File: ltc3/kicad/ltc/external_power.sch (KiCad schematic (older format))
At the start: 44 parts, among them M501 1A, M502 1A, M503 1A, M504 1A, P503 MicroFit header, P504 MicroFit connector, P505 MicroFit header, P506 MicroFit connector, P507 PowerPole, P508 PowerPole, P509 PowerPole, P510 PowerPole, P511 PowerPole, P512 PowerPole, P513 PowerPole, P514 PowerPole, Q501 PMV45EN, Q502 PMV45EN, Q503 PMV45EN, Q504 PMV45EN, SW501 MOMENTARY, SW502 MOMENTARY, SW503 MOMENTARY, SW504 MOMENTARY, U501 TLP3542, U502 TLP3542, U503 TLP3542, U504 TLP3542

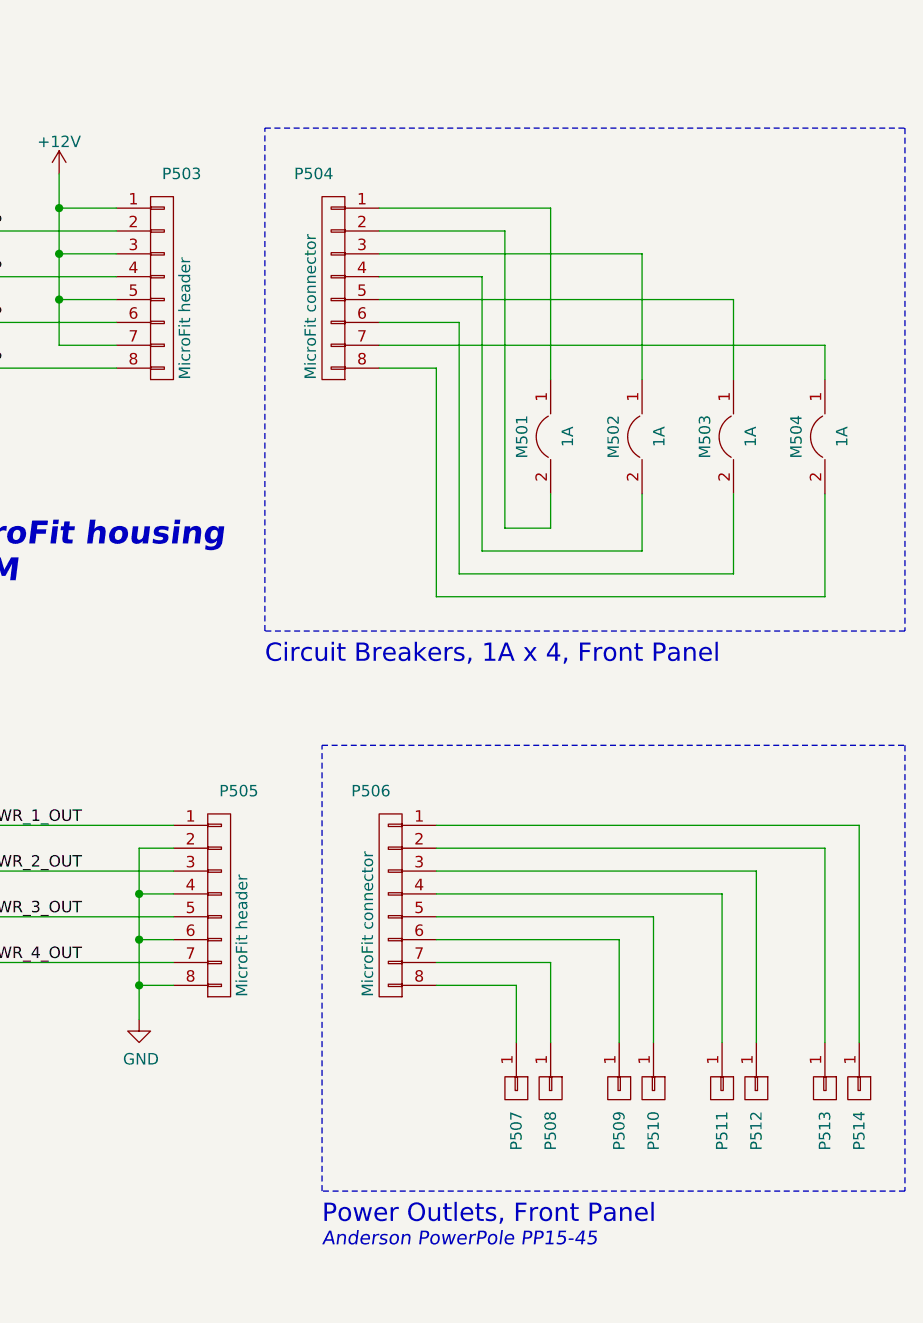
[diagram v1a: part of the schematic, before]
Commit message: LTC3: LTC BOM and PCB changes.
1. Added RJ45 connector outline to BeagleBone footprint.

2. Rotated BeagleBone footprint on PCB, so that the RJ45 connector
   is on a board edge.

3. Added a notch to the board for BeagleBone RJ45 jack clearance.

4. Updated PCB footprint annotations to align with changes made to the
   LTC schematic in the past few months.

5. Changed BAKERCON MOSFETs to be same part used to activate ignition
   relays.  (Fewer distinct components on the board.)
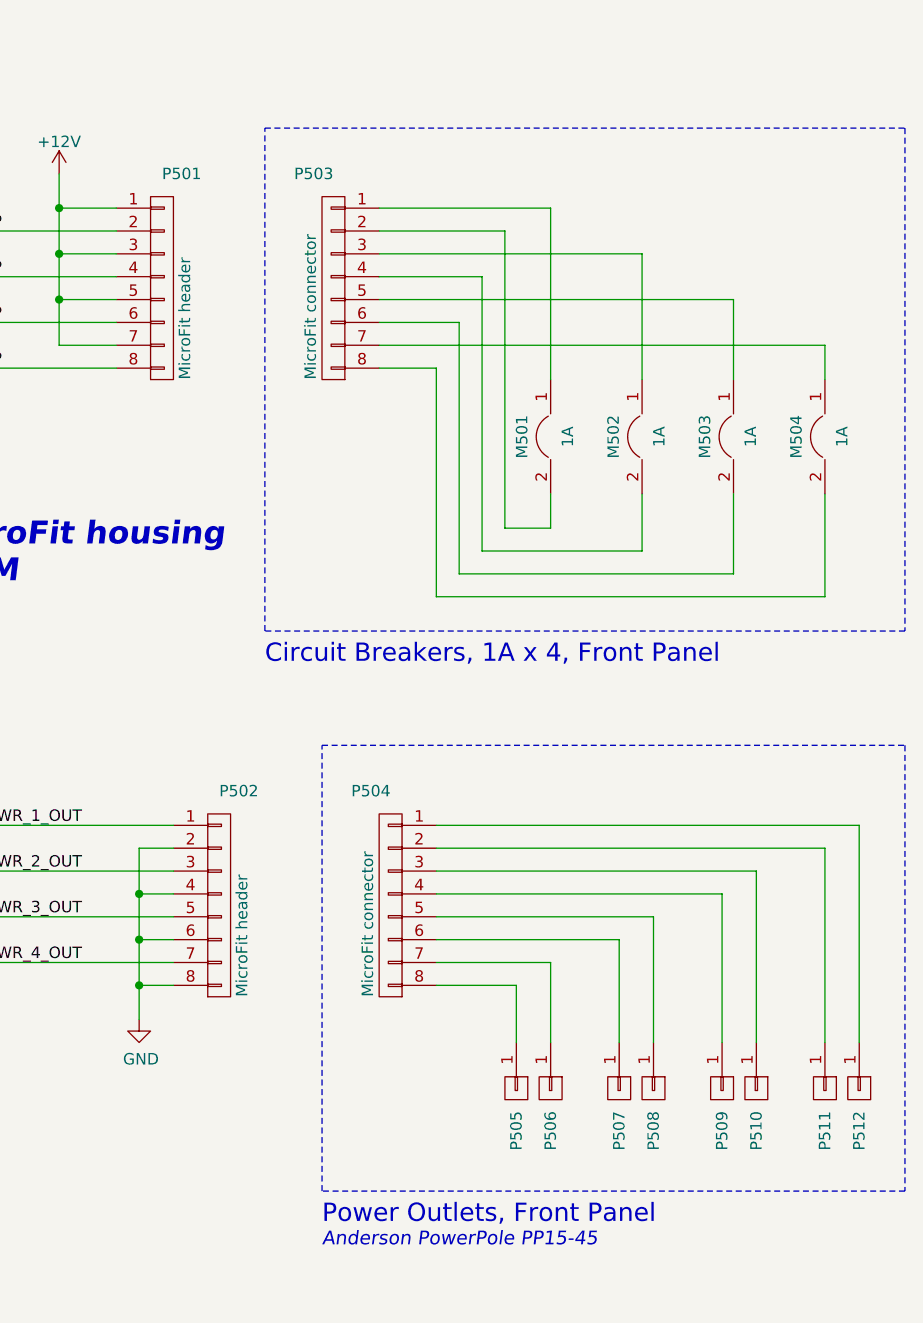
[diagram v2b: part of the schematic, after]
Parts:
- P501: renamed from P503; Note to front panel -> to front panel; mates to P503
- P502: renamed from P505; Note to front panel -> to front panel; mates to P502
- P503: renamed from P504; Note OFF-BOARD; mates to P503 -> OFF-BOARD; mates to P501
- P504: renamed from P506; Note OFF-BOARD; mates to P505 -> OFF-BOARD; mates to P502
- renumbered P507 to P505, P508 to P506, P509 to P507, P510 to P508, P511 to P509, P512 to P510, P513 to P511, P514 to P512

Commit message: Converted LTC schematic from KiCad v4 to v5.
v5 schematic exported as PDF to
build/schematics/3-Launch_Tower_Computer-KiCad_v5.pdf to simplify
comparison and sanity-checking versus the v4 version at
build/schematics/3-Launch_Tower_Computer.pdf.  New version should be
mv'd overtop of old version before merging this branch to *master*.
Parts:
- C501, C502, C503, C504: symbol C -> Device:C
- M501, M502, M503, M504: symbol BREAKER_1P -> breakers:BREAKER_1P
- P501, P502, P503, P504: symbol CONN_01X08 -> Connector:Conn_01x08_Male
- P505, P506, P507, P508, P509, P510, P511, P512: symbol CONN_01X01 -> Connector:Conn_01x01_Male
- Q501, Q502, Q503, Q504: symbol PMV45EN -> PMV45EN:PMV45EN
- R501, R502, R503, R504, R505, R506, R507, R508, R509, R510, R511, R512: symbol R -> Device:R
- SW501, SW502, SW503, SW504: symbol SW_PUSH_SMALL -> Switch:SW_Push
- U501, U502, U503, U504: symbol TLP3542 -> TLP:TLP3542
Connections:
- net GND: now also SW501.1, SW502.1, SW503.1, SW504.1; no longer SW501.2, SW502.2, SW503.2, SW504.2
- net at Q501.3 (D), U501.2: now also SW501.2; no longer SW501.1
- net at Q502.3 (D), U502.2: now also SW502.2; no longer SW502.1
- net at Q504.3 (D), U504.2: now also SW504.2; no longer SW504.1
- net at Q503.3 (D), U503.2: now also SW503.2; no longer SW503.1
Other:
- moved on the sheet: SW501, SW502, SW503, SW504
